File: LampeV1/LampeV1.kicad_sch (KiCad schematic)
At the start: 15 parts, among them J1 Screw_Terminal_01x06, J2 Screw_Terminal_01x04, J3 Conn_01x05_Male, J4 Conn_01x04_Male, Q7 BT136-500, U1 ESP32-S2-DevKitM, U2 STA301a, U3 EL817, U4 MOC3020M, U5 R-78B5.0-2.0

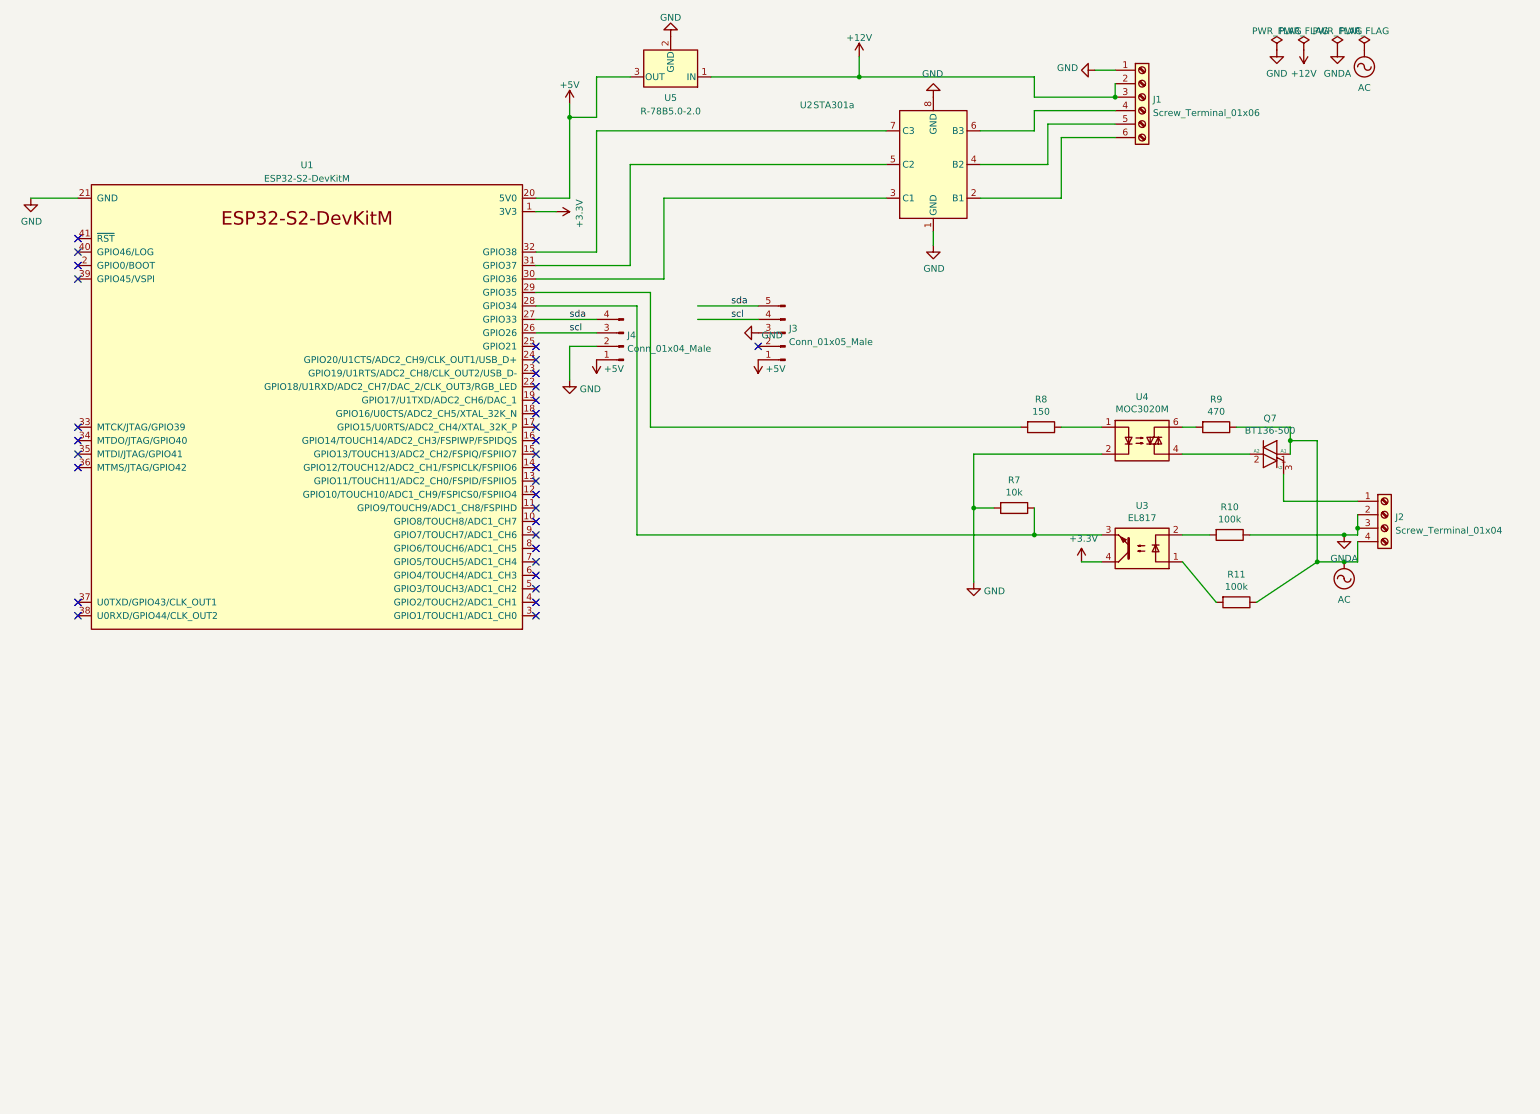
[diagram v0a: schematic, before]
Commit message: added case
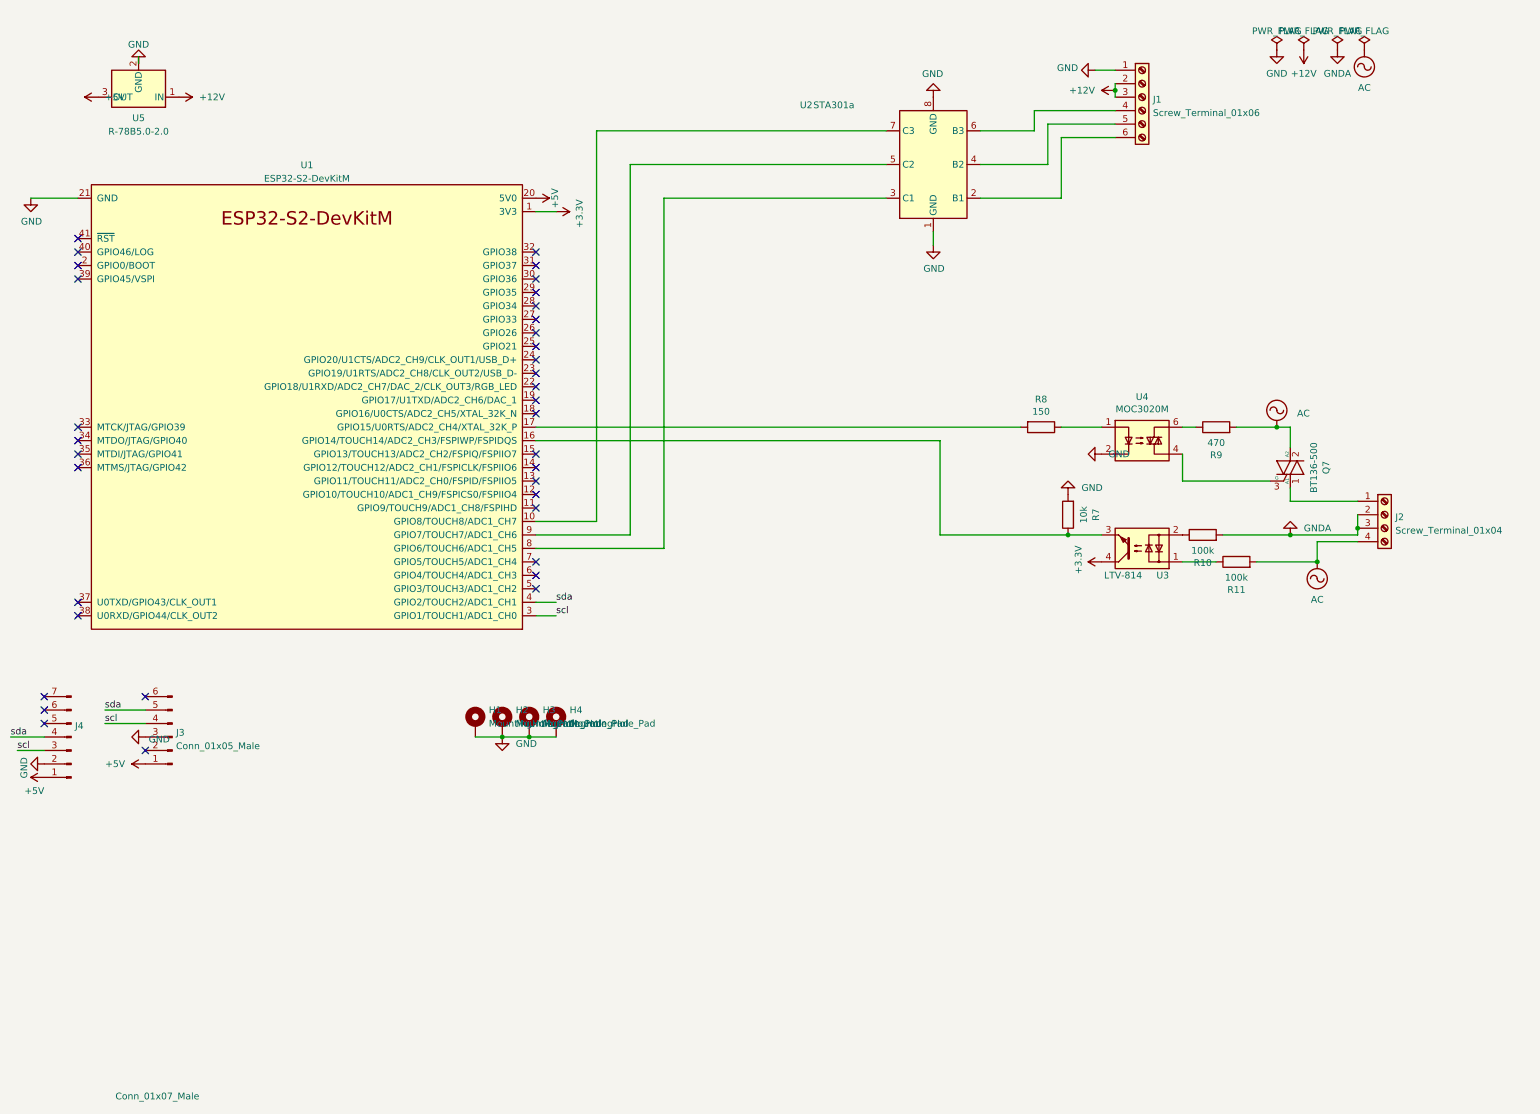
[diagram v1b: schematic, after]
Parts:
- added H1, H2, H3, H4: MountingHole_Pad, MountingHole:MountingHole_2.7mm_M2.5_ISO14580_Pad_TopBottom, symbol Mechanical:MountingHole_Pad
- J1: footprint TerminalBlock_Phoenix:TerminalBlock_Phoenix_MKDS-1,5-6_1x06_P5.00mm_Horizontal -> TerminalBlock_MetzConnect:TerminalBlock_MetzConnect_Type094_RT03506HBLU_1x06_P5.00mm_Horizontal
- J2: footprint TerminalBlock_Phoenix:TerminalBlock_Phoenix_MKDS-1,5-4_1x04_P5.00mm_Horizontal -> TerminalBlock_MetzConnect:TerminalBlock_MetzConnect_Type094_RT03504HBLU_1x04_P5.00mm_Horizontal
- J3: footprint Connector_PinHeader_2.54mm:PinHeader_1x05_P2.54mm_Vertical -> manual:LTR390; symbol Connector:Conn_01x05_Male -> Connector:Conn_01x06_Male
- J4: value Conn_01x04_Male -> Conn_01x07_Male; footprint Connector_PinHeader_2.54mm:PinHeader_1x04_P2.54mm_Vertical -> manual:scd30; symbol Connector:Conn_01x04_Male -> Connector:Conn_01x07_Male
- R10, R11, R7, R8, R9: footprint Resistor_THT:R_Axial_DIN0414_L11.9mm_D4.5mm_P15.24mm_Horizontal -> Resistor_THT:R_Axial_DIN0207_L6.3mm_D2.5mm_P7.62mm_Horizontal
- U3: value EL817 -> LTV-814; symbol Isolator:EL817 -> Isolator:LTV-814
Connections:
- net AC: now also Q7.2 (A2), R11.2, R9.2; no longer Q7.1 (A1), R11.1, R9.1
- net GND: now also H1.1, H2.1, H3.1, H4.1
- net GNDA: now also R10.2; no longer R10.1
- net scl: now also U1.3 (GPIO1/TOUCH1/ADC1_CH0); no longer U1.26 (GPIO26)
- net sda: now also U1.4 (GPIO2/TOUCH2/ADC1_CH1); no longer U1.27 (GPIO33)
- net at U3.1: now also R11.1; no longer R11.2
- net at U3.2: now also R10.1; no longer R10.2
- net at R7.1, U3.3: now also U1.16 (GPIO14/TOUCH14/ADC2_CH3/FSPIWP/FSPIDQS); no longer U1.28 (GPIO34)
- net at U4.4: now also Q7.3 (G); no longer Q7.2 (A2)
- net at U4.6: now also R9.1; no longer R9.2
- net at J2.1 (Pin_1): now also Q7.1 (A1); no longer Q7.3 (G)
- net at R8.2: now also U1.17 (GPIO15/U0RTS/ADC2_CH4/XTAL_32K_P); no longer U1.29 (GPIO35)
- net at U1.10 (GPIO8/TOUCH8/ADC1_CH7): now also U2.7 (C3)
- net at U1.30 (GPIO36): no longer U2.3 (C1)
- net at U1.31 (GPIO37): no longer U2.5 (C2)
- net at U1.32 (GPIO38): no longer U2.7 (C3)
- net at U1.8 (GPIO6/TOUCH6/ADC1_CH5): now also U2.3 (C1)
- net at U1.9 (GPIO7/TOUCH7/ADC1_CH6): now also U2.5 (C2)
- no-connect marks 32 -> 36
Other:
- moved on the sheet: Q7, R10, R11, R7, R9, U5
